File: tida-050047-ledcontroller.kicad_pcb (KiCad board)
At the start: 4 copper layers, 50 x 175 mm, 114 parts, among them Q1 AOD424, Q2 AOD424, U1 TPS25750DRJKR, U10 XT30PW-F, U15 SB1045L_C2844167, U16 BQ7790400PWR, U17 SMTSO3015CTJ, U18 SMTSO3015CTJ, U19 SMTSO3015CTJ, U2 CAT24C256WI-GT3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

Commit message: fix commit
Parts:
- C30, C31, C41: footprint Capacitor_SMD:C_0603_1608Metric_Pad1.08x0.95mm_HandSolder -> Capacitor_SMD:C_0402_1005Metric_Pad0.74x0.62mm_HandSolder
- C37, C38: footprint Capacitor_SMD:C_0603_1608Metric_Pad1.08x0.95mm_HandSolder -> Capacitor_SMD:C_0402_1005Metric_Pad0.74x0.62mm_HandSolder; moved to B.Cu
- moved C46 51.0 mm to (196.5, 155.8), turned to -90 degrees
- moved C45 48.0 mm to (195.0, 155.8), turned to -90 degrees
- moved C44 45.0 mm to (193.5, 155.8), turned to -90 degrees
- moved C43 42.0 mm to (192.0, 155.8), turned to -90 degrees
- moved L2 41.4 mm to (186.5, 150.8), turned to 0 degrees
- moved C48 40.9 mm to (195.6, 160.4), turned to -90 degrees
- moved C47 39.1 mm to (194.1, 160.4), turned to -90 degrees
- moved C42 38.9 mm to (190.4, 155.8), turned to -90 degrees
- moved C40 37.3 mm to (192.5, 160.4), turned to -90 degrees
- moved R14 37.1 mm to (195.2, 164.4), turned to 90 degrees
- moved C41 34.6 mm to (187.6, 157.2), turned to 0 degrees
- moved C37 33.5 mm to (184.6, 160.1), turned to -90 degrees
- moved C38 32.9 mm to (188.4, 160.0), turned to 90 degrees
- moved R13 32.5 mm to (191.0, 160.4), turned to -90 degrees
- moved C30 32.3 mm to (185.4, 157.2), turned to 0 degrees
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
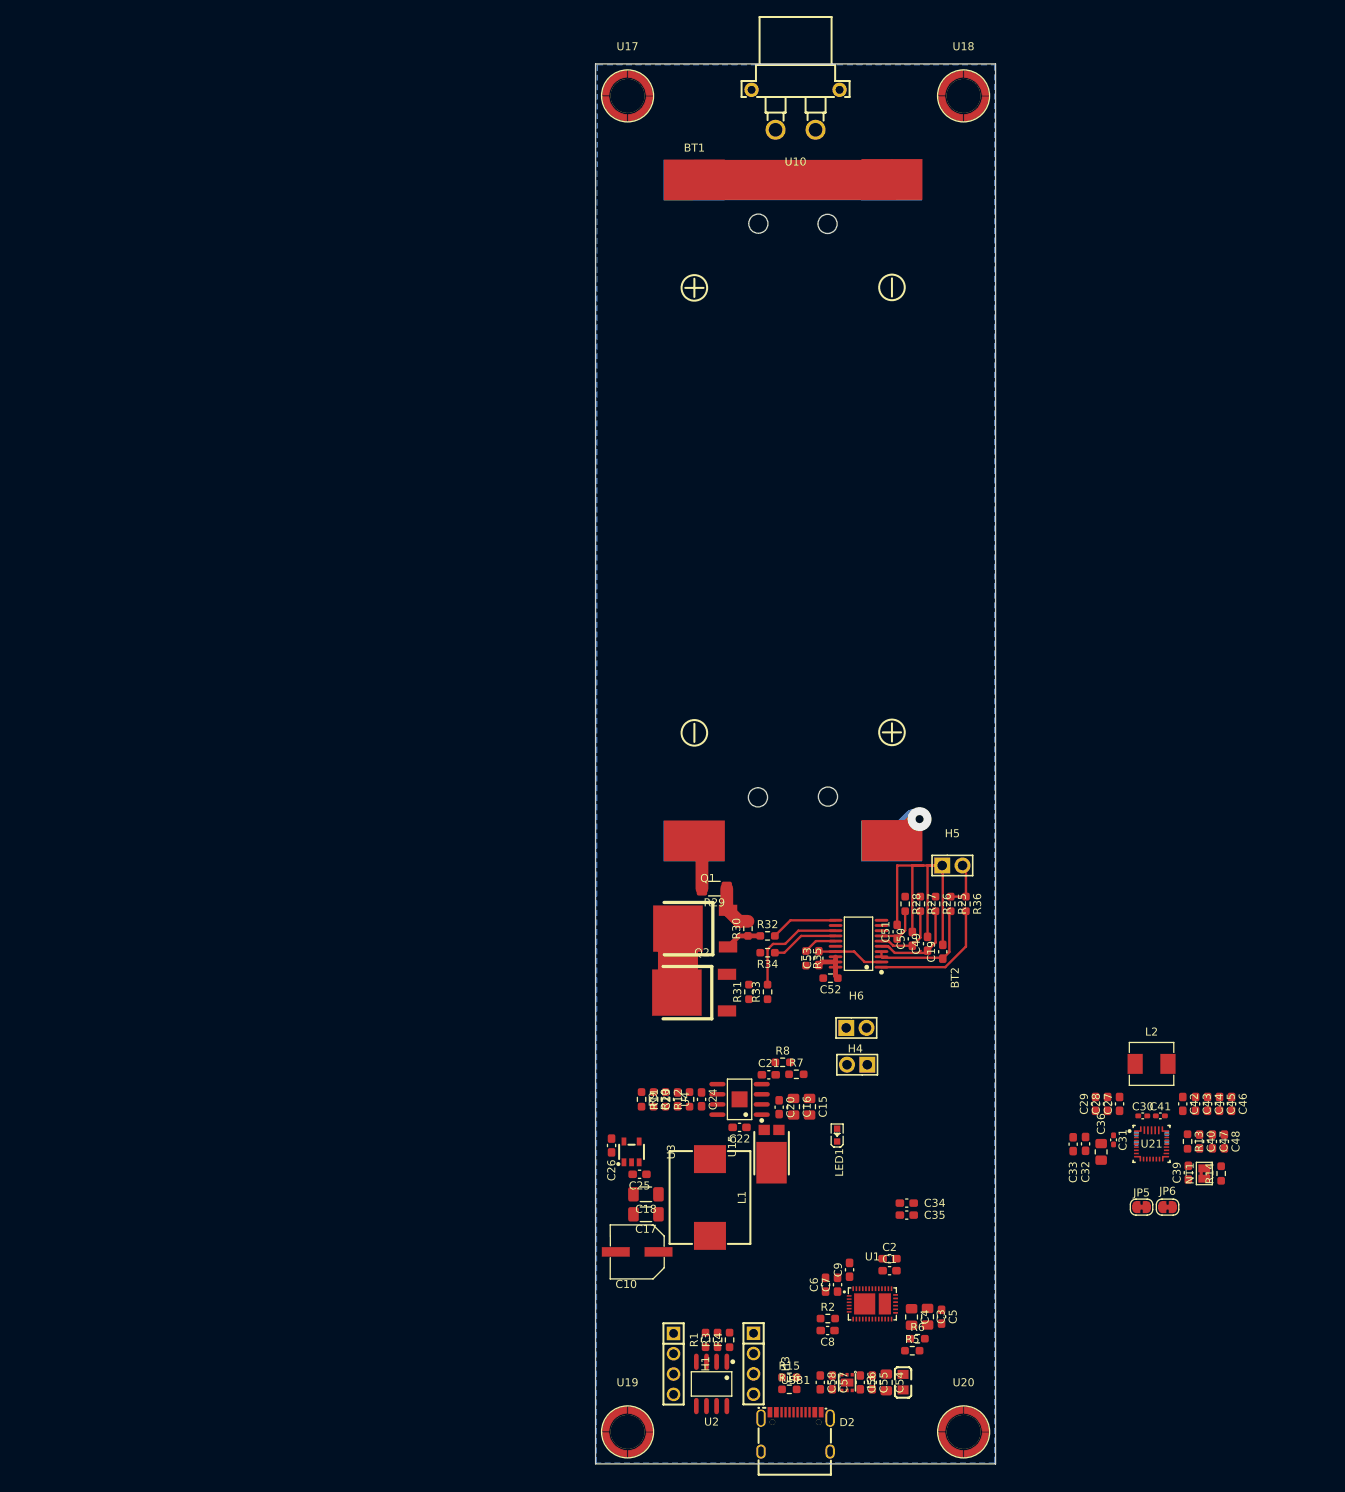
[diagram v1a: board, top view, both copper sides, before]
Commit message: fix zones with via stiching
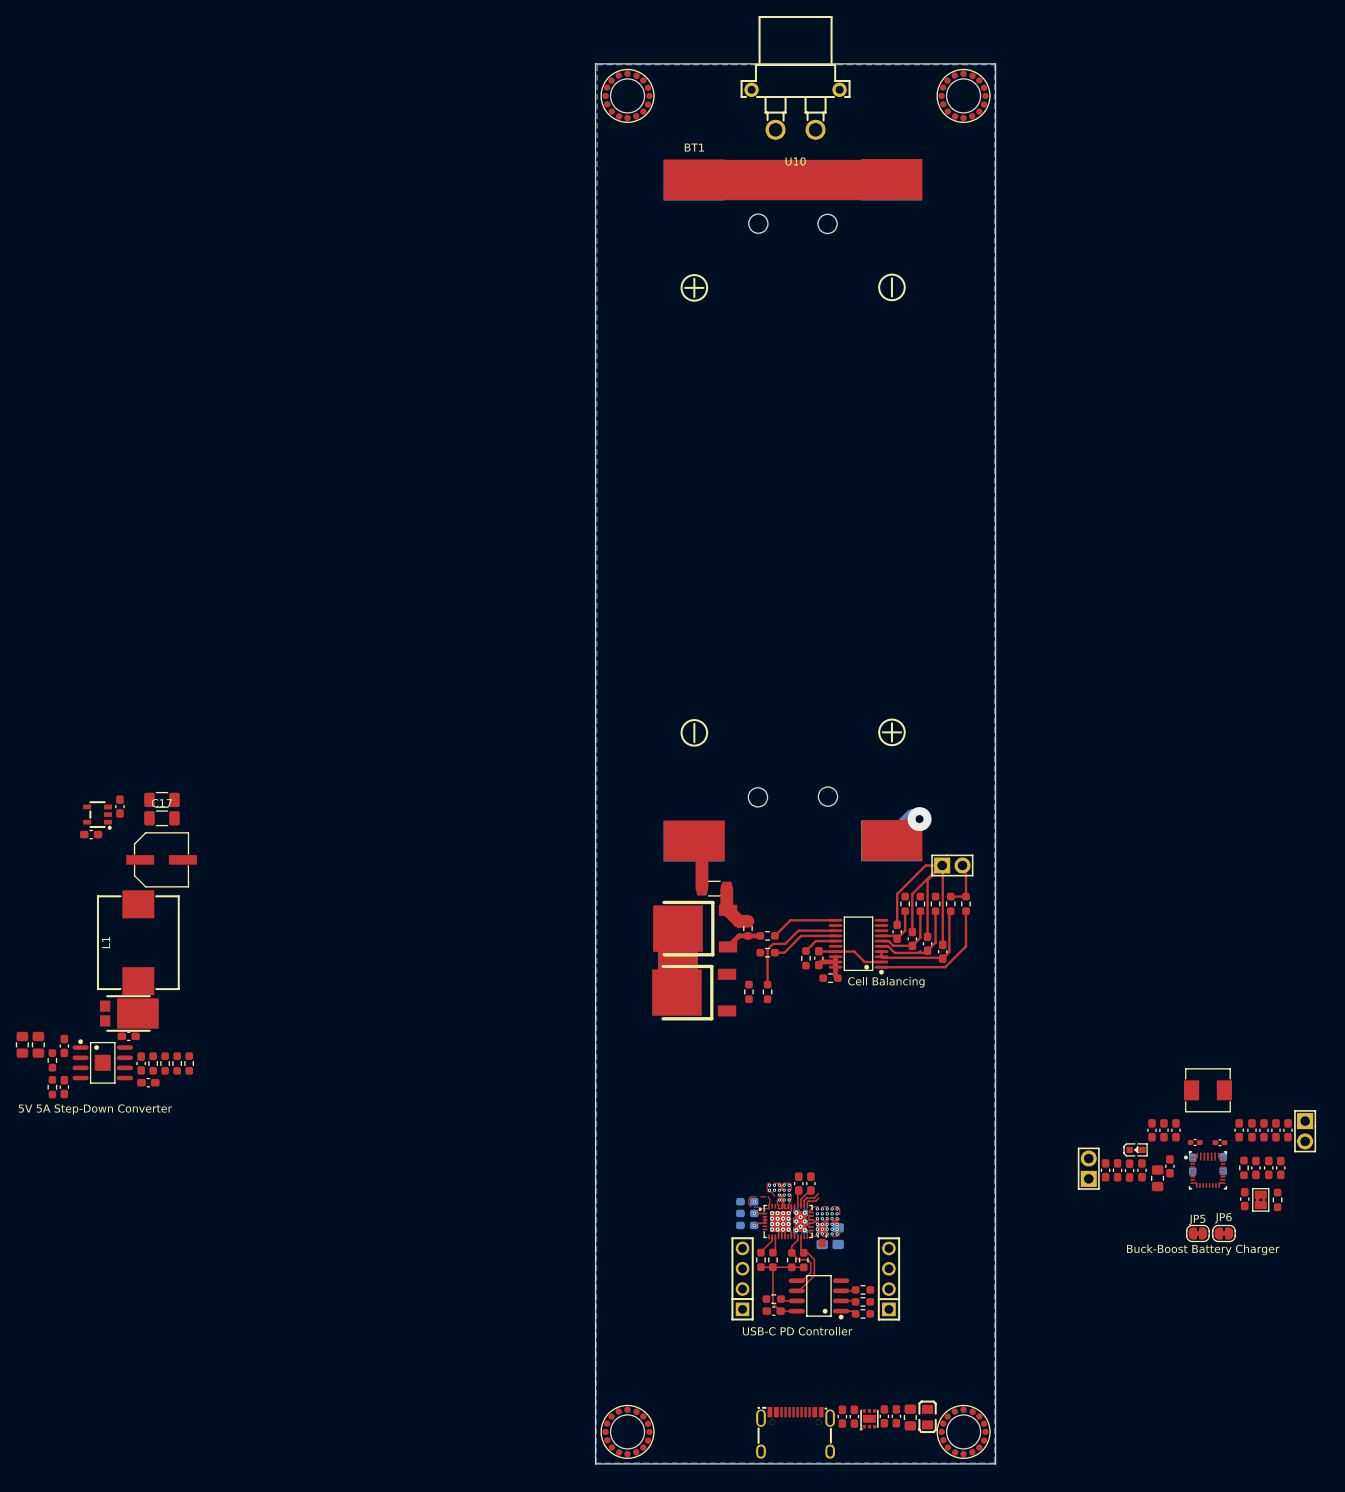
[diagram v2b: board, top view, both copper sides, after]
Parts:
- C3, C4, C6, C7, C9: moved to B.Cu
- C31, C37, C38: footprint Capacitor_SMD:C_0402_1005Metric_Pad0.74x0.62mm_HandSolder -> Capacitor_SMD:C_0603_1608Metric_Pad1.08x0.95mm_HandSolder
- U17, U18, U19, U20: footprint easyeda2kicad:SMD_BD5.6-L5.6-W5.6-D4.1 -> easyeda2kicad:SMTSO3030CTJ
- moved C15 98.7 mm to (45.4, 148.4), turned to 90 degrees
- moved C16 94.7 mm to (47.4, 148.4), turned to 90 degrees
- moved R7 93.0 mm to (49.1, 150.3), turned to 90 degrees
- moved R8 91.3 mm to (49.1, 153.7), turned to 90 degrees
- moved C20 89.7 mm to (50.6, 148.5), turned to 90 degrees
- moved C21 88.1 mm to (50.6, 153.7), turned to -90 degrees
- moved U15 82.9 mm to (57.8, 144.4), turned to 180 degrees
- moved U4 79.7 mm to (55.4, 150.6), turned to -90 degrees
- moved C25 79.6 mm to (57.5, 118.6), turned to -90 degrees
- moved U3 79.0 mm to (54.8, 119.6), turned to 0 degrees
- moved L1 78.2 mm to (59.9, 135.6), turned to 90 degrees
- moved C17 78.2 mm to (62.8, 120.0), turned to 0 degrees
- moved C18 78.0 mm to (62.8, 117.8), turned to 0 degrees
- moved C22 77.2 mm to (58.6, 147.3), turned to 0 degrees
- moved C10 77.0 mm to (62.8, 125.2), turned to 0 degrees
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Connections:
- C1 pad 1: C_CC1 -> C_CC2
- U1 pad 29: C_CC1 -> C_CC2
- USB1 pad B5: C_CC1 -> C_CC2
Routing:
- net LDO_3V3: track 0.00 -> 14.6 mm, vias 0 -> 1
- net GND: track 0.00 -> 11.0 mm, vias 0 -> 16
- net I2C_SCL: track 0.00 -> 8.83 mm
- net I2C_SDA: track 0.00 -> 8.57 mm
- net -BATT: track 54.8 -> 51.9 mm
- net C_USB_N: track 0.00 -> 2.84 mm
- net C_CC1: track 0.00 -> 2.57 mm
- net I2C1_SDA: track 0.00 -> 2.57 mm
- net LDO_1V5: track 0.00 -> 2.28 mm, vias 0 -> 1
- net C_USB_P: track 0.00 -> 2.16 mm
- net I2C1_SCL: track 0.00 -> 2.11 mm
- net Net-(U2-WP): track 0.00 -> 2.06 mm
- net C_CC2: track 0.00 -> 2.03 mm
- net Net-(U2-A0): track 0.00 -> 1.96 mm
- net Net-(U2-A2): track 0.00 -> 1.87 mm
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- added copper zone on B.Cu, net DRAIN
- added copper zone on F.Cu, net P3V3
- added copper zone on F.Cu, net PP5V
- added copper zone on F.Cu, net PPHV
- added copper zone on F.Cu, net VBUS
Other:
- board text added: "5V 5A Step-Down Converter"
- board text added: "Buck-Boost Battery Charger"
- board text added: "Cell Balancing"
- board text added: "USB-C PD Controller"

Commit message: add pcb layout using the layout guidelines froms the texas instruments ICs
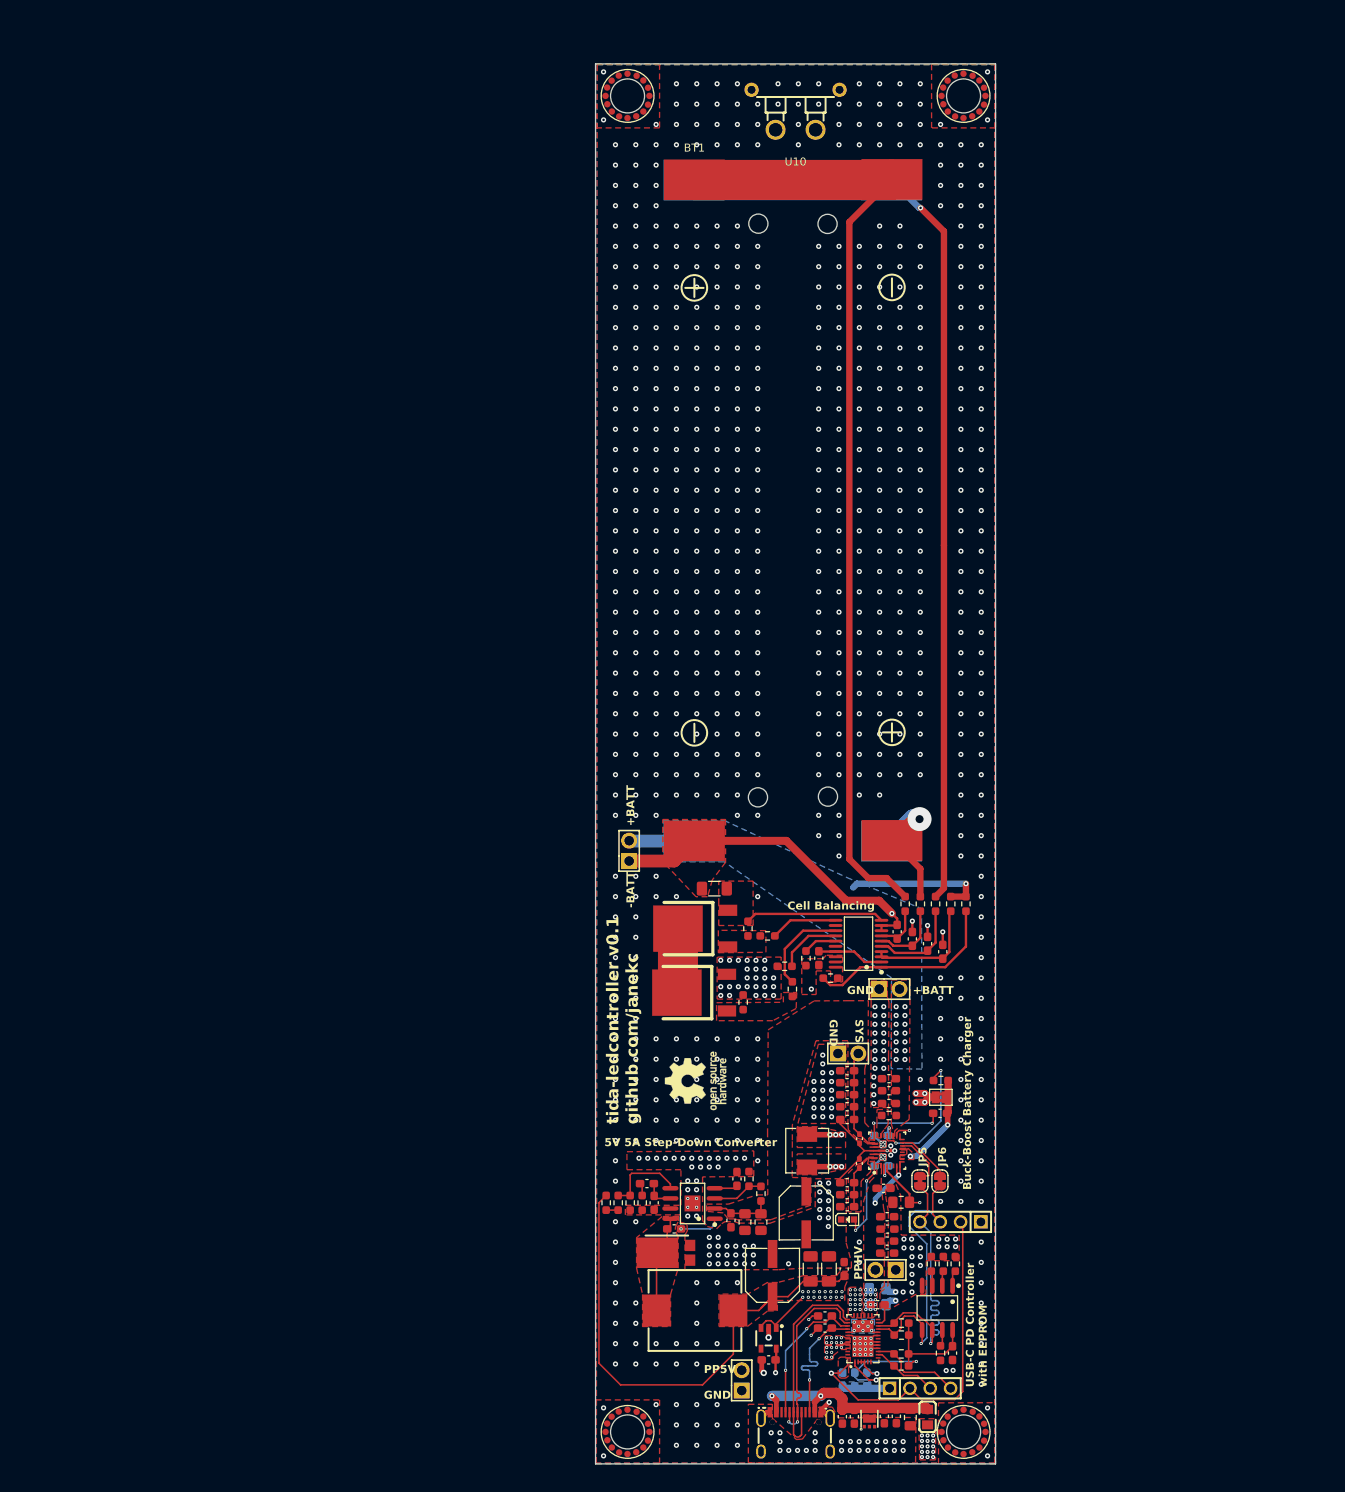
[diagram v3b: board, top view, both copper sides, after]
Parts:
- added C11: OVZ101M1CTR-0606, easyeda2kicad:CAP-SMD_BD6.3-L6.6-W6.6-FD-A, F.Cu at (143.3, 169.4)
- added H2: PZ254V-11-02P, easyeda2kicad:HDR-TH_2P-P2.54-V-M, F.Cu at (153.7, 141.4)
- added H7: PZ254V-11-02P, easyeda2kicad:HDR-TH_2P-P2.54-V-M, F.Cu at (135.3, 190.3)
- moved C25 107.4 mm to (148.1, 176.4), turned to 90 degrees
- moved C26 107.2 mm to (138.6, 187.8), turned to 0 degrees
- moved U3 106.4 mm to (138.6, 185.1), turned to 90 degrees
- moved C18 101.9 mm to (146.2, 176.4), turned to 90 degrees
- moved C17 98.7 mm to (143.9, 176.4), turned to 90 degrees
- moved C15 94.9 mm to (137.7, 170.5), turned to -90 degrees
- moved C10 92.4 mm to (139.1, 177.2), turned to 90 degrees
- moved C16 91.1 mm to (135.7, 170.5), turned to -90 degrees
- moved R7 90.1 mm to (137.7, 167.0), turned to -90 degrees
- moved R8 87.8 mm to (136.2, 165.1), turned to -90 degrees
- moved C20 86.1 mm to (133.9, 170.3), turned to -90 degrees
- moved C21 84.9 mm to (134.7, 165.1), turned to 90 degrees
- moved L1 83.4 mm to (129.4, 181.6), turned to 0 degrees
- moved U4 75.8 mm to (129.1, 168.2), turned to 90 degrees
- moved U15 75.2 mm to (126.8, 174.4), turned to 0 degrees
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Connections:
- C36 pad 2: REGN -> ILIM_HIZ
- U17 pad 1: unconnected-(U17-Pad1) -> GND
- U18 pad 1: unconnected-(U18-Pad1) -> GND
- U19 pad 1: unconnected-(U19-Pad1) -> GND
- U20 pad 1: unconnected-(U20-Pad1) -> GND
- U21 pad 5: REGN -> ILIM_HIZ
- USB1 pad B1A12: (no net) -> GND
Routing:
- net PP5V: track 0.00 -> 232.1 mm, vias 8 -> 24
- net Net-(BT1-Pad2): track 24.7 -> 120.8 mm
- net Net-(BT3-Pad2): track 24.7 -> 117.5 mm, vias 0 -> 1
- net P3V3: track 0.00 -> 55.7 mm, vias 1 -> 2
- net GND: track 11.0 -> 53.5 mm, vias 16 -> 905
- net I2C_SDA: track 8.57 -> 37.4 mm, vias 0 -> 1
- net I2C_SCL: track 8.83 -> 37.5 mm, vias 0 -> 1
- net Net-(C54-Pad2): track 0.00 -> 26.2 mm, vias 0 -> 2
- net C_USB_P: track 2.16 -> 26.8 mm
- net C_USB_N: track 2.84 -> 23.7 mm, vias 0 -> 2
- net SYS: track 0.00 -> 20.5 mm
- net +BATT: track 5.97 -> 25.9 mm, vias 0 -> 15
- net ILIM_HIZ: track 0.00 -> 19.4 mm, vias 0 -> 2
- net -BATT: track 51.9 -> 69.0 mm, vias 0 -> 5
- net PROG: track 0.00 -> 16.5 mm, vias 0 -> 2
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- added copper zone on B.Cu, net +BATT
- added copper zone on F.Cu, net +BATT
- added copper zone on F.Cu, net -BATT
- added copper zone on F.Cu, net AGND
- added copper zone on F.Cu, net GND
- added copper zone on In1.Cu, net GND
- added copper zone on In2.Cu, net GND
- added copper zone on F.Cu, net Net-(Q1-G)
- added copper zone on F.Cu, net Net-(Q1-S)
- added copper zone on F.Cu, net Net-(Q2-G)
- added copper zone on F.Cu, net Net-(R13-Pad1)
- added copper zone on B.Cu, net Net-(U21-SW1)
- added copper zone on F.Cu, net Net-(U21-SW1)
- added copper zone on B.Cu, net Net-(U21-SW2)
- added copper zone on F.Cu, net Net-(U21-SW2)
- added copper zone on F.Cu, net Net-(U4-PH)
- added copper zone on F.Cu, net PMID
- added copper zone on In2.Cu, net PP5V
- added copper zone on F.Cu, net SYS
- added copper zone on In2.Cu, net VBUS
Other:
- board text added: "+BATT"
- board text added: "-BATT"
- board text added: "GND"
- board text added: "PP5V GND"
- board text added: "PPHV"
- board text added: "SYS GND"
- board text added: "USB-C PD Controller with EEPROM"
- board text added: "tida-ledcontroller v0.1 github.com/janekc"
- board text removed: "USB-C PD Controller"
